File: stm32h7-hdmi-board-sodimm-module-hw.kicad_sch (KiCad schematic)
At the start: 0 parts

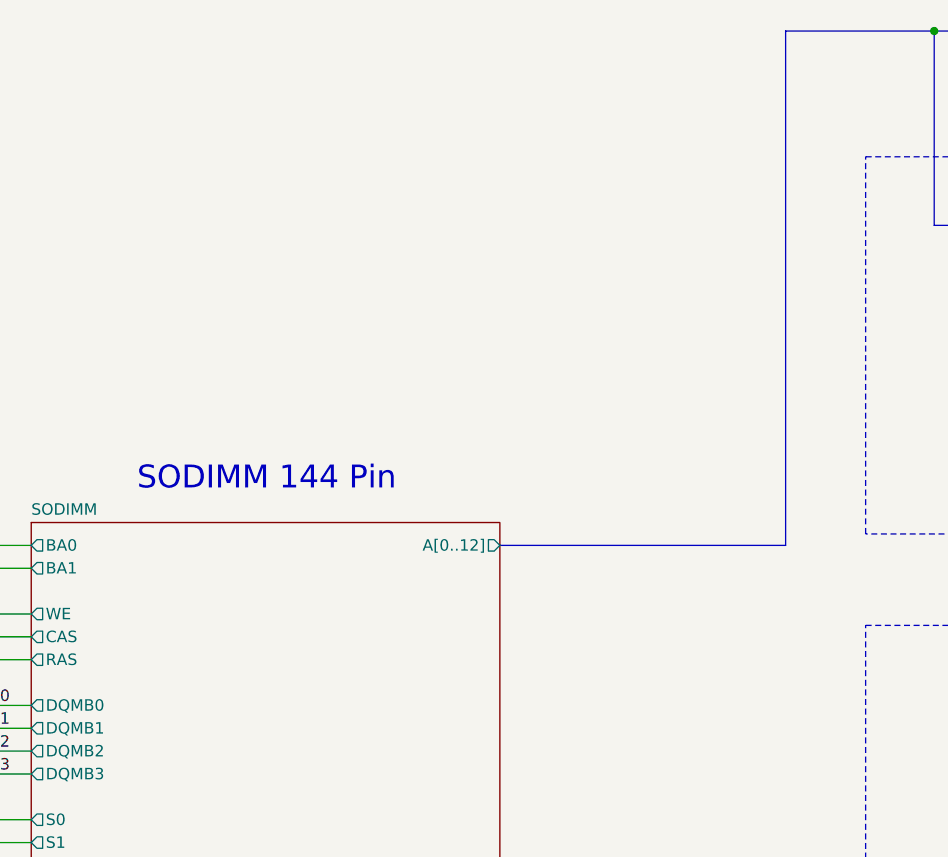
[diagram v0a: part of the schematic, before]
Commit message: [#100650] Add EEPROM memory IC for Serial Presence Detection
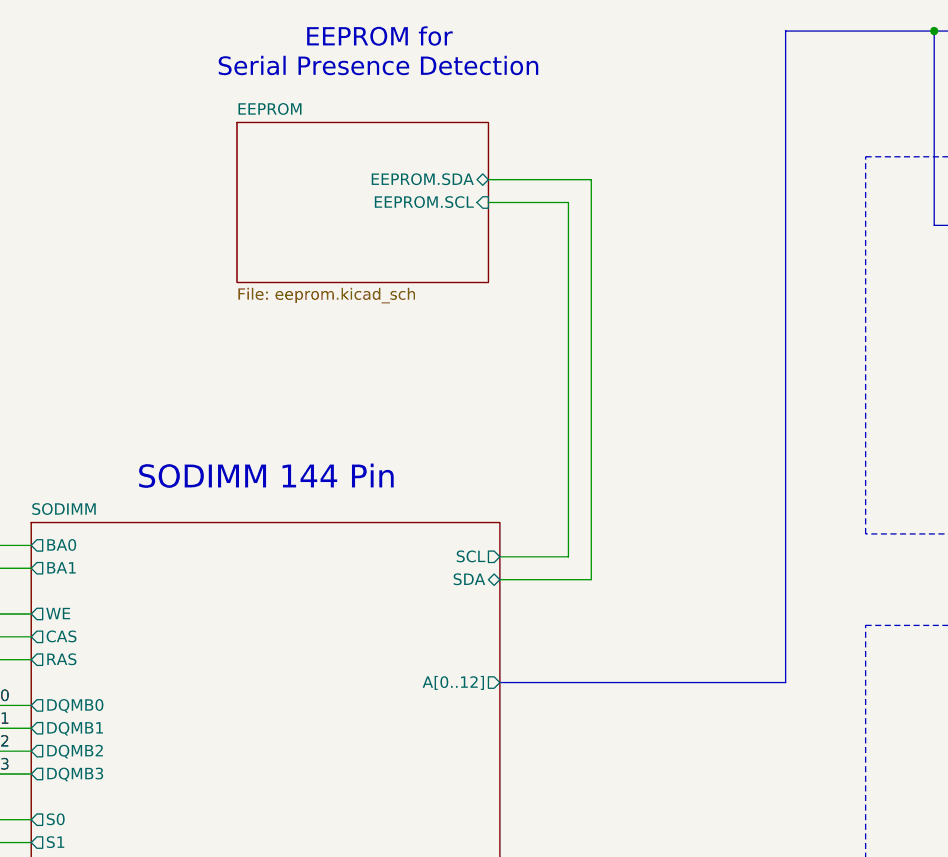
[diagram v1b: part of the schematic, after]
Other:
- added sheet EEPROM (eeprom.kicad_sch)
- sheet SODIMM ports: added SCL, SDA; removed none
- note added: "EEPROM for Serial Presence Detection"
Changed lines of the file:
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@@
 	(title_block
 		(title "STM32H7 HDMI Board SODIMM")
-		(date "2026-07-13")
+		(date "2026-07-14")
 		(rev "1.0.0")
 		(company "Antmicro Ltd")
@@
 			(font
 				(size 2.54 2.54)
+			)
+		)
+	)
+	(text "EEPROM for \nSerial Presence Detection"
+		(exclude_from_sim no)
+		(at 75.438 66.04 0)
+		(effects
+			(font
+				(size 2.032 2.032)
 			)
 		)
@@
 	(wire
 		(pts
+			(xy 99.06 124.46) (xy 88.9 124.46)
+		)
+		(stroke
+			(width 0)
+			(type default)
+		)
+	)
+	(wire
+		(pts
 			(xy 27.94 161.29) (xy 36.83 161.29)
 		)
@@
 	(bus
 		(pts
-			(xy 88.9 120.65) (xy 120.65 120.65)
+			(xy 88.9 135.89) (xy 120.65 135.89)
 		)
 		(stroke
@@
 		)
 	)
+	(wire
+		(pts
+			(xy 87.63 80.01) (xy 99.06 80.01)
+		)
+		(stroke
+			(width 0)
+			(type default)
+		)
+	)
 	(bus
 		(pts
@@
 	(bus
 		(pts
-			(xy 120.65 120.65) (xy 120.65 63.5)
+			(xy 120.65 135.89) (xy 120.65 63.5)
 		)
 		(stroke
@@
 	(wire
 		(pts
+			(xy 99.06 80.01) (xy 99.06 124.46)
+		)
+		(stroke
+			(width 0)
+			(type default)
+		)
+	)
+	(wire
+		(pts
 			(xy 195.58 113.03) (xy 203.2 113.03)
 		)
@@
 		)
 	)
+	(wire
+		(pts
+			(xy 96.52 121.92) (xy 96.52 82.55)
+		)
+		(stroke
+			(width 0)
+			(type default)
+		)
+	)
 	(bus
 		(pts
@@
 	(wire
 		(pts
+			(xy 96.52 82.55) (xy 87.63 82.55)
+		)
+		(stroke
+			(width 0)
+			(type default)
+		)
+	)
+	(wire
+		(pts
 			(xy 245.11 160.02) (xy 252.73 160.02)
 		)
@@
 		(pts
 			(xy 295.91 92.71) (xy 303.53 92.71)
+		)
+		(stroke
+			(width 0)
+			(type default)
+		)
+	)
+	(wire
+		(pts
+			(xy 88.9 121.92) (xy 96.52 121.92)
 		)
 		(stroke
@@
 		(polyline
 			(pts
-				(xy 77.47 118.11) (xy 91.44 118.11) (xy 91.44 128.27) (xy 77.47 128.27)
+				(xy 77.47 133.35) (xy 91.44 133.35) (xy 91.44 143.51) (xy 77.47 143.51)
 			)
 			(stroke
@@
 		(length 2.54)
 		(shape round)
-		(at 90.17 118.11 0)
-		(fields_autoplaced yes)
+		(at 90.17 133.35 0)
 		(effects
 			(font
@@
 		)
 		(property "Netclass" "55Ohm-se_ADDR"
-			(at 90.8685 115.57 0)
+			(at 90.8685 130.81 0)
 			(show_name no)
 			(do_not_autoplace no)
@@
 		)
 		(property "Component Class" ""
-			(at -86.36 0 0)
+			(at -86.36 15.24 0)
 			(show_name no)
 			(do_not_autoplace no)
@@
 					(size 1.27 1.27)
 					(italic yes)
+				)
+			)
+		)
+	)
+	(sheet
+		(at 59.69 73.66)
+		(size 27.94 17.78)
+		(exclude_from_sim no)
+		(in_bom yes)
+		(on_board yes)
+		(dnp no)
+		(fields_autoplaced yes)
+		(stroke
+			(width 0.1524)
+			(type solid)
+		)
+		(fill
+			(color 0 0 0 0)
+		)
+		(property "Sheetname" "EEPROM"
+			(at 59.69 72.9484 0)
+			(show_name no)
+			(do_not_autoplace no)
+			(effects
+				(font
+					(size 1.27 1.27)
+				)
+				(justify left bottom)
+			)
+		)
+		(property "Sheetfile" "eeprom.kicad_sch"
+			(at 59.69 92.0246 0)
+			(show_name no)
+			(do_not_autoplace no)
+			(effects
+				(font
+					(size 1.27 1.27)
+				)
+				(justify left top)
+			)
+		)
+		(pin "EEPROM.SCL" input
+			(at 87.63 82.55 0)
+			(effects
+				(font
+					(size 1.27 1.27)
+				)
+				(justify right)
+			)
+		)
+		(pin "EEPROM.SDA" bidirectional
+			(at 87.63 80.01 0)
+			(effects
+				(font
+					(size 1.27 1.27)
+				)
+				(justify right)
+			)
+		)
+		(instances
+			(project "stm32h7-hdmi-board-sodimm-module-hw"
+				(path "/92fcd7c5-798f-49cd-ae80-ce2fa78a6354"
+					(page "11")
 				)
 			)
@@
 		)
 		(pin "A[0..12]" output
-			(at 88.9 120.65 0)
+			(at 88.9 135.89 0)
 			(effects
 				(font
@@
 			(effects
 				(font
+					(size 1.27 1.27)
+				)
+				(justify right)
+			)
+		)
+		(pin "SCL" output
+			(at 88.9 121.92 0)
+			(effects
+				(font
+					(size 1.27 1.27)
+				)
+				(justify right)
+			)
+		)
+		(pin "SDA" bidirectional
+			(at 88.9 124.46 0)
+			(effects
+				(font

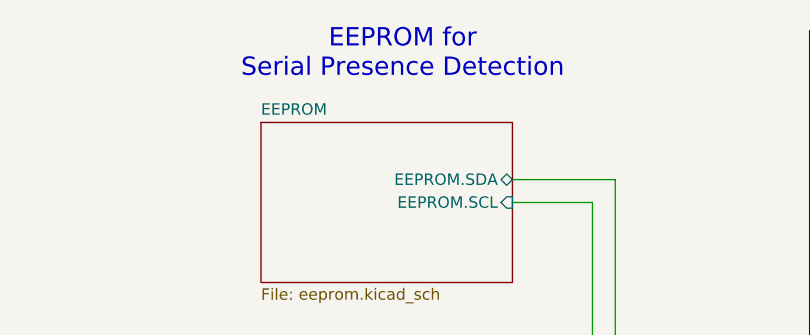
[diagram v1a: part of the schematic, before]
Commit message: [#100650] Change EEPROM memory IC
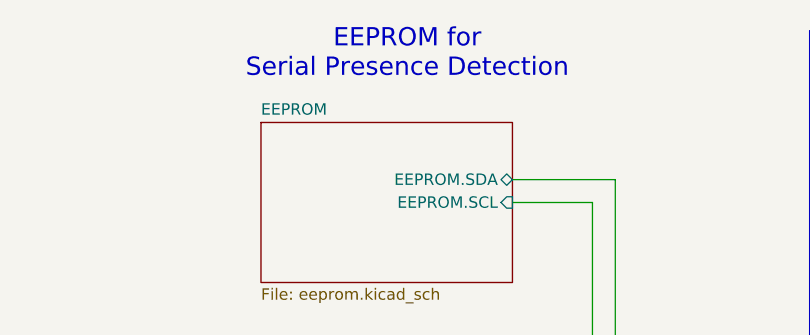
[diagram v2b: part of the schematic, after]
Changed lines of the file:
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@@
 	(text "EEPROM for \nSerial Presence Detection"
 		(exclude_from_sim no)
-		(at 75.438 66.04 0)
+		(at 75.946 66.04 0)
 		(effects
 			(font

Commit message: [#100650] Update schematic labels, add bulk cap
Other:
- sheet SDR ports: added ~{CAS}, ~{CS}, ~{RAS}, ~{WE}; removed NCAS, NCS, NRAS, NWE
- sheet SDR1 ports: added ~{CAS}, ~{CS}, ~{RAS}, ~{WE}; removed NCAS, NCS, NRAS, NWE
- sheet SDR2 ports: added ~{CAS}, ~{CS}, ~{RAS}, ~{WE}; removed NCAS, NCS, NRAS, NWE
- sheet SDR3 ports: added ~{CAS}, ~{CS}, ~{RAS}, ~{WE}; removed NCAS, NCS, NRAS, NWE
- sheet SDR4 ports: added ~{CAS}, ~{CS}, ~{RAS}, ~{WE}; removed NCAS, NCS, NRAS, NWE
- sheet SDR5 ports: added ~{CAS}, ~{CS}, ~{RAS}, ~{WE}; removed NCAS, NCS, NRAS, NWE
- sheet SDR6 ports: added ~{CAS}, ~{CS}, ~{RAS}, ~{WE}; removed NCAS, NCS, NRAS, NWE
- sheet SDR7 ports: added ~{CAS}, ~{CS}, ~{RAS}, ~{WE}; removed NCAS, NCS, NRAS, NWE
- note added: "Rank0 4 x IS42S86400F-7TL 4x16Mx32bit (256MB)"
- note added: "Rank1 4 x IS42S86400F-7TL 4x16Mx32bit (256MB)"
- note added: "SDRAM SODIMM Module for STM32H747: IS42S86400F-7TL memory organization: 4x16Mx8bit Module memory organization: 512MB 2Rx8 (32 bit data bus)"
- note removed: "Physical Bank 1 4 x IS42S86400F-7TL 4x16Mx32bit (256MB)"
- note removed: "Physical Bank 2 4 x IS42S86400F-7TL 4x16Mx32bit (256MB)"
- note removed: "STM32H747 SDRAM controller: 2 SDRAM banks: 4x16Mx32bit (256MB) IS42S86400F-7TL memory organization: 4x16Mx8bit 4 parallel ICs makes 32bit data bus (4x16Mx32bit)"

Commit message: [#100650] Schematic cleanup
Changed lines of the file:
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@@
+	)
+	(junction
+		(at 185.42 165.1)
+		(diameter 0)
+		(color 0 0 0 0)
 	)
 	(junction
@@
 	)
 	(junction
-		(at 185.42 165.1)
-		(diameter 0)
-		(color 0 0 0 0)
-	)
-	(junction
 		(at 238.76 165.1)
 		(diameter 0)
@@
 	)
 	(junction
-		(at 185.42 187.96)
-		(diameter 0)
-		(color 0 0 0 0)
-	)
-	(junction
 		(at 191.77 63.5)
 		(diameter 0)
@@
 		)
 	)
-	(bus
-		(pts
-			(xy 185.42 187.96) (xy 115.57 187.96)
-		)
-		(stroke
-			(width 0)
-			(type default)
-		)
-	)
 	(wire
 		(pts
@@
 	(bus
 		(pts
+			(xy 185.42 182.88) (xy 185.42 165.1)
+		)
+		(stroke
+			(width 0)
+			(type default)
+		)
+	)
+	(bus
+		(pts
 			(xy 229.87 113.03) (xy 238.76 113.03)
 		)
@@
 	(bus
 		(pts
+			(xy 119.38 182.88) (xy 185.42 182.88)
+		)
+		(stroke
+			(width 0)
+			(type default)
+		)
+	)
+	(bus
+		(pts
 			(xy 176.53 165.1) (xy 185.42 165.1)
 		)
@@
 		)
 	)
-	(bus
-		(pts
-			(xy 185.42 165.1) (xy 185.42 187.96)
-		)
-		(stroke
-			(width 0)
-			(type default)
-		)
-	)
 	(wire
 		(pts
@@
 	(bus
 		(pts
-			(xy 238.76 187.96) (xy 185.42 187.96)
-		)
-		(stroke
+			(xy 115.57 187.96) (xy 238.76 187.96)
+		)
+		(stroke

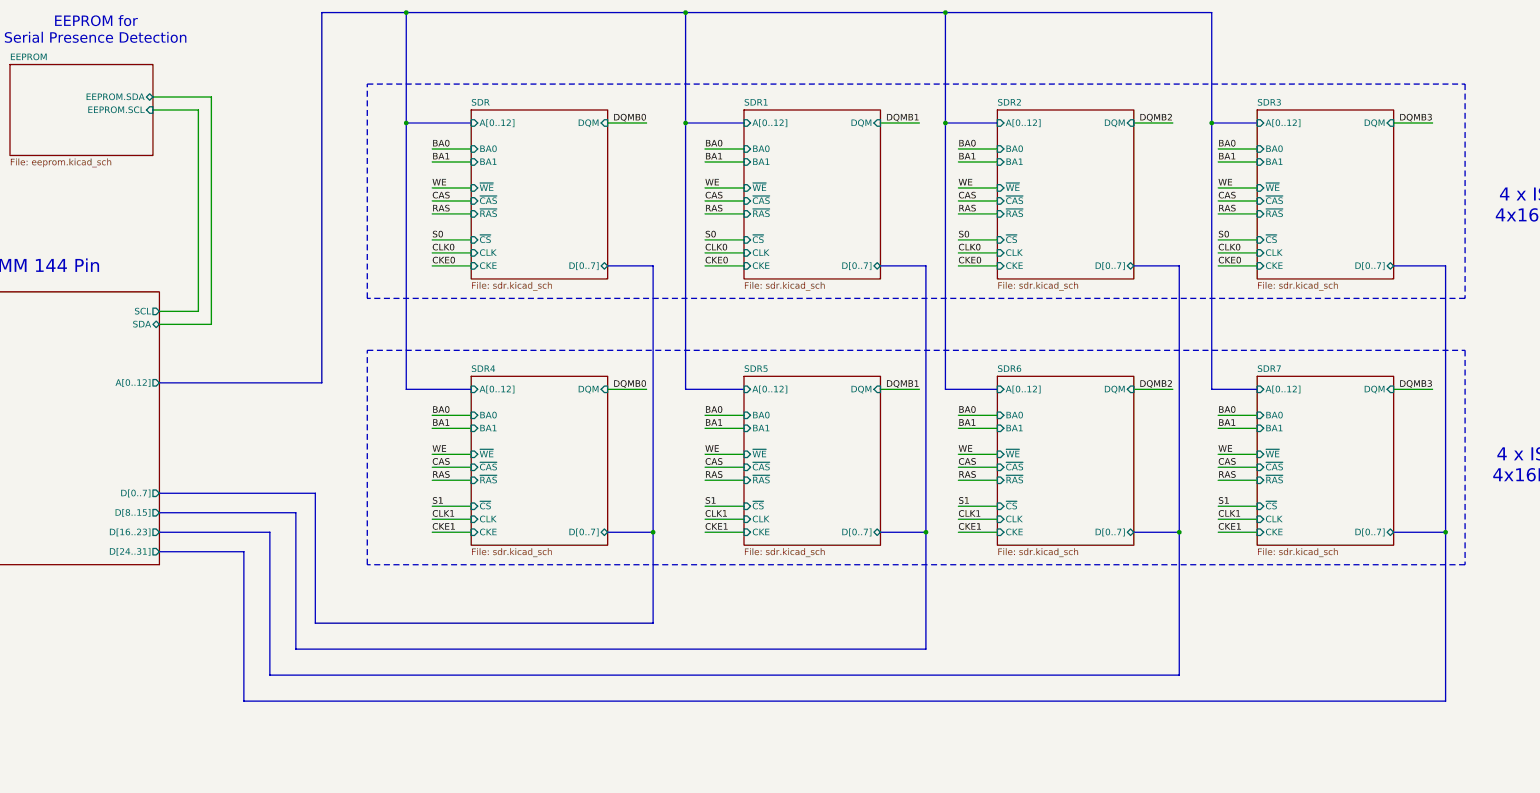
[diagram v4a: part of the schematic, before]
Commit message: [#100919] Route data bus
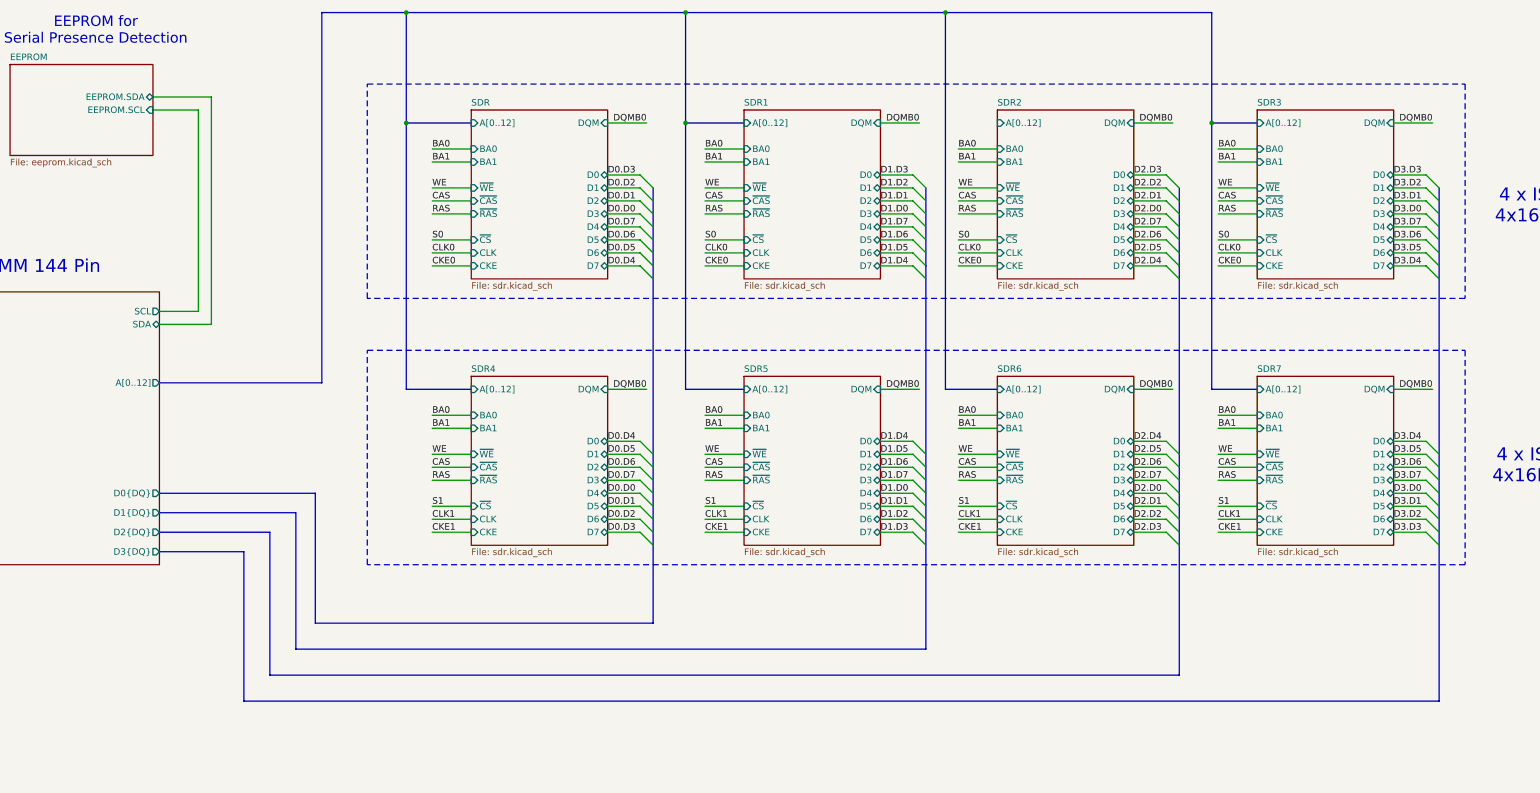
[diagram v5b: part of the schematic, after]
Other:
- sheet SDR ports: added D0, D1, D2, D3, D4, D5, D6, D7; removed D[0..7]
- sheet SDR1 ports: added D0, D1, D2, D3, D4, D5, D6, D7; removed D[0..7]
- sheet SDR2 ports: added D0, D1, D2, D3, D4, D5, D6, D7; removed D[0..7]
- sheet SDR3 ports: added D0, D1, D2, D3, D4, D5, D6, D7; removed D[0..7]
- sheet SDR4 ports: added D0, D1, D2, D3, D4, D5, D6, D7; removed D[0..7]
- sheet SDR5 ports: added D0, D1, D2, D3, D4, D5, D6, D7; removed D[0..7]
- sheet SDR6 ports: added D0, D1, D2, D3, D4, D5, D6, D7; removed D[0..7]
- sheet SDR7 ports: added D0, D1, D2, D3, D4, D5, D6, D7; removed D[0..7]
- sheet SODIMM ports: added D0{DQ}, D1{DQ}, D2{DQ}, D3{DQ}; removed D[0..7], D[16..23], D[24..31], D[8..15]
